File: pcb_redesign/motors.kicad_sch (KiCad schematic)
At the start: 8 parts

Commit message: schematic imported
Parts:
- A3908EEETR-T1, A3908EEETR-T3: footprint (none) -> motor_driver_ic:PSON50P200X300X60-9N
- M1, M3: footprint (none) -> motor:motor
- R4, R8: footprint (none) -> 18k_ohm_0603:RESC1608X55N
- R5, R9: footprint (none) -> 10k_ohm_0603:RESC1508X50N
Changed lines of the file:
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@@
       (effects (font (size 1.27 1.27)))
     )
-    (property "Footprint" "" (at 81.28 123.19 0)
+    (property "Footprint" "motor_driver_ic:PSON50P200X300X60-9N" (at 81.28 123.19 0)
       (effects (font (size 1.27 1.27)) hide)
     )
@@
       (effects (font (size 1.27 1.27)))
     )
-    (property "Footprint" "" (at 82.55 55.88 0)
+    (property "Footprint" "motor_driver_ic:PSON50P200X300X60-9N" (at 82.55 55.88 0)
       (effects (font (size 1.27 1.27)) hide)
     )
@@
       (effects (font (size 1.27 1.27)) (justify left))
     )
-    (property "Footprint" "" (at 54.102 138.43 90)
+    (property "Footprint" "18k_ohm_0603:RESC1608X55N" (at 54.102 138.43 90)
       (effects (font (size 1.27 1.27)) hide)
     )
@@
       (effects (font (size 1.27 1.27)))
     )
-    (property "Footprint" "" (at 114.3 128.27 0)
+    (property "Footprint" "motor:motor" (at 114.3 128.27 0)
       (effects (font (size 1.27 1.27)) hide)
     )
@@
       (effects (font (size 1.27 1.27)))
     )
-    (property "Footprint" "" (at 115.57 60.96 0)
+    (property "Footprint" "motor:motor" (at 115.57 60.96 0)
       (effects (font (size 1.27 1.27)) hide)
     )
@@
       (effects (font (size 1.27 1.27)) (justify left))
     )
-    (property "Footprint" "" (at 54.102 148.59 90)
+    (property "Footprint" "10k_ohm_0603:RESC1508X50N" (at 54.102 148.59 90)
       (effects (font (size 1.27 1.27)) hide)
     )
@@
       (effects (font (size 1.27 1.27)) (justify left))
     )
-    (property "Footprint" "" (at 55.372 81.28 90)
+    (property "Footprint" "10k_ohm_0603:RESC1508X50N" (at 55.372 81.28 90)
       (effects (font (size 1.27 1.27)) hide)
     )
@@
       (effects (font (size 1.27 1.27)) (justify left))
     )
-    (property "Footprint" "" (at 55.372 71.12 90)
-      (effects (font (size 1.27 1.27)) hide)
-    )
+    (property "Footprint" "18k_ohm_0603:RESC1608X55N" (at 55.372 71.12 90)
+      (effects (font (size 1.27 1.27)) hide)
+    )

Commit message: components added to board
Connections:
- net 3.7_UNREG: now reaches A3908EEETR-T3.3 (VDD)
- net 3.7_UNREG: now also A3908EEETR-T1.3 (VDD)
- net ENA Left motor renamed ENA Left Motor
- net ENA Left Motor: no longer A3908EEETR-T3.6 (IN_1)
- net ENA Right motor renamed ENB Right Motor
- net ENB Right motor renamed ENA Right Motor
- new net ENB Left Motor: A3908EEETR-T3.6 (IN_1)
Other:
- moved on the sheet: M3

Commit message: switching to laptop
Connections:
- net 3.7_UNREG: no longer A3908EEETR-T3.3 (VDD)
- new net VCC_3V3: A3908EEETR-T3.3 (VDD)
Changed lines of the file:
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@@
     )
   )
-  (global_label "3.7_UNREG" (shape input) (at 93.98 132.08 0) (fields_autoplaced)
+  (global_label "VCC_3V3" (shape input) (at 93.98 132.08 0) (fields_autoplaced)
     (effects (font (size 1.27 1.27)) (justify left))
-    (property "Intersheetrefs" "${INTERSHEET_REFS}" (at 107.2272 132.08 0)
+    (property "Intersheetrefs" "${INTERSHEET_REFS}" (at 104.9896 132.08 0)
       (effects (font (size 1.27 1.27)) (justify left) hide)
     )

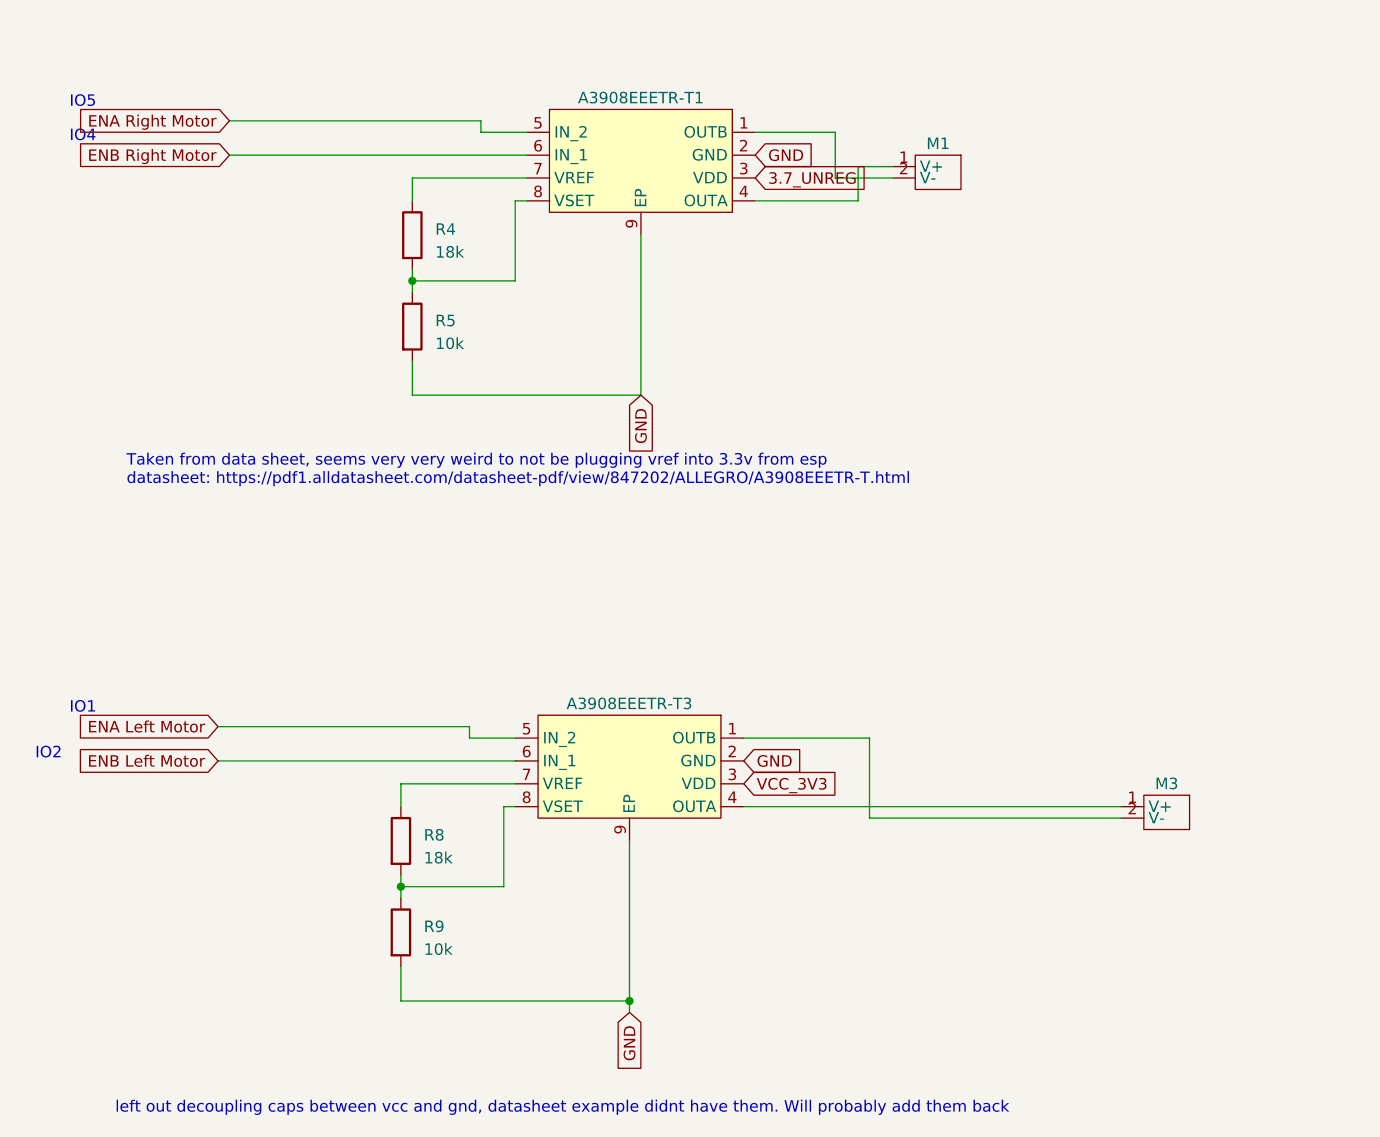
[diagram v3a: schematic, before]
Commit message: wired up 2.13
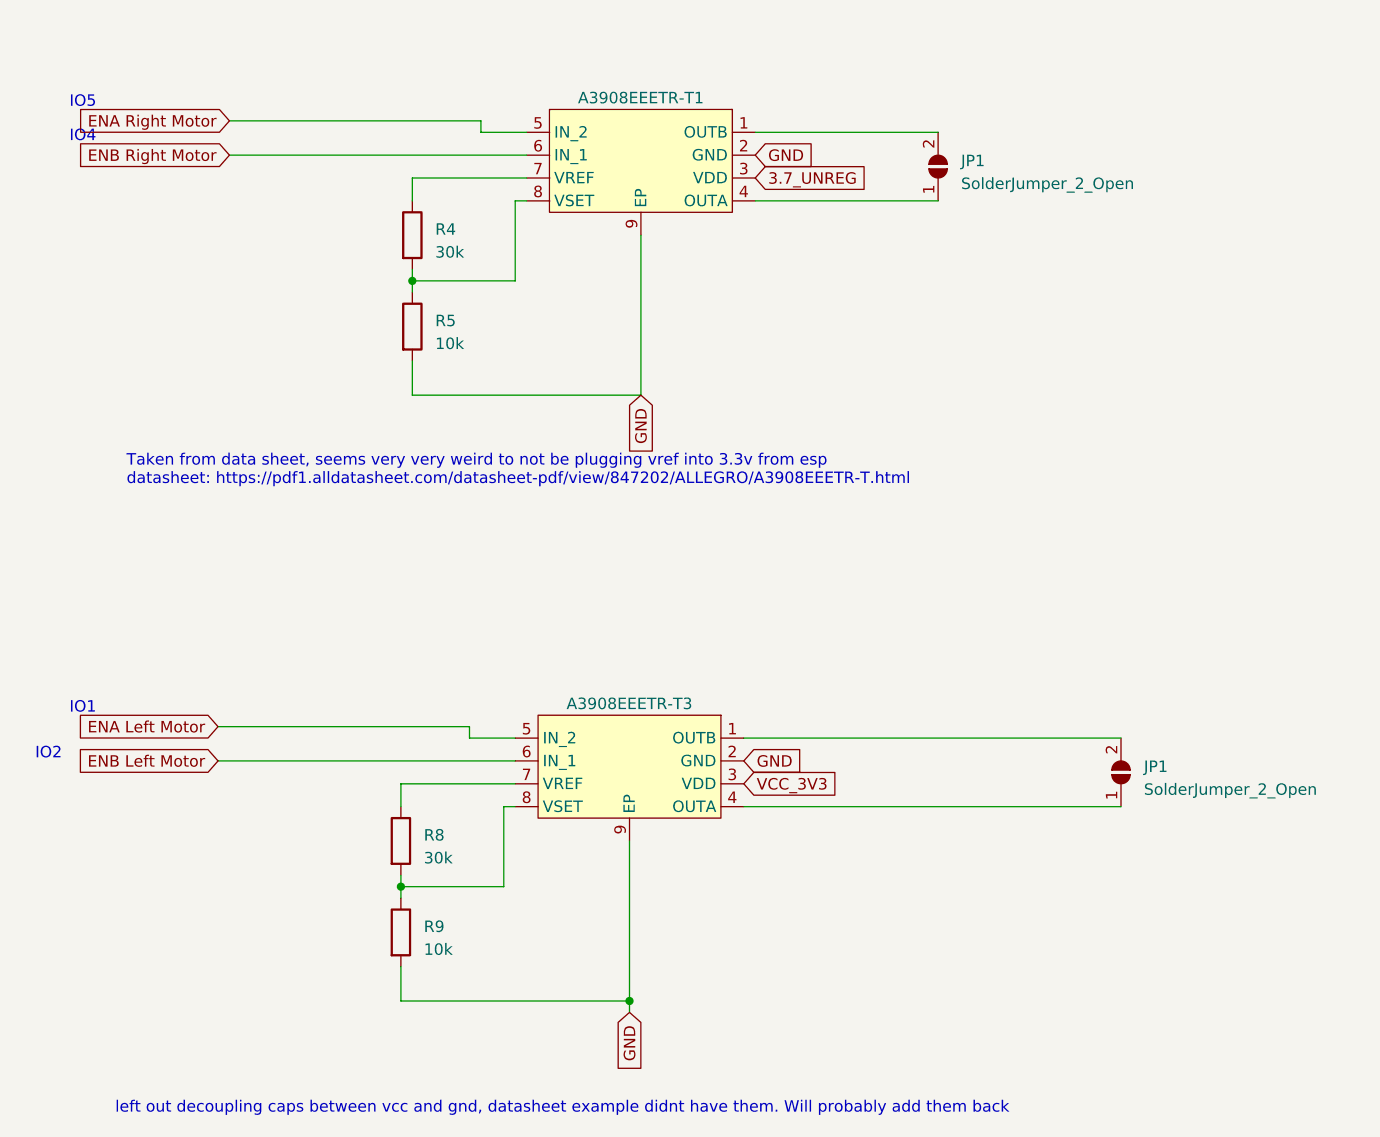
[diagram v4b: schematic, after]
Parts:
- removed M1, M3: ~, motor:motor, symbol lib:motor
- added JP1 (x2): SolderJumper_2_Open, Jumper:SolderJumper-2_P1.3mm_Open_Pad1.0x1.5mm, symbol Jumper:SolderJumper_2_Open
- R4, R8: value 18k -> 30k
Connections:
- net at A3908EEETR-T3.1 (OUTB): now also JP1.2 (B)
- net at A3908EEETR-T3.4 (OUTA): now also JP1.1 (A)
- net at A3908EEETR-T1.1 (OUTB): now also JP1.2 (B)
- net at A3908EEETR-T1.4 (OUTA): now also JP1.1 (A)
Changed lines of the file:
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@@
-    (stroke (width 0) (type default))
-  )
-  (wire (pts (xy 95.25 59.69) (xy 104.14 59.69))
     (stroke (width 0) (type default))
   )
@@
     (stroke (width 0) (type default))
   )
-  (wire (pts (xy 104.14 64.77) (xy 110.49 64.77))
-    (stroke (width 0) (type default))
-  )
   (wire (pts (xy 55.88 142.24) (xy 55.88 143.51))
     (stroke (width 0) (type default))
@@
     (stroke (width 0) (type default))
   )
-  (wire (pts (xy 106.68 67.31) (xy 106.68 63.5))
-    (stroke (width 0) (type default))
-  )
   (wire (pts (xy 64.77 58.42) (xy 64.77 59.69))
     (stroke (width 0) (type default))
   )
-  (wire (pts (xy 95.25 67.31) (xy 106.68 67.31))
+  (wire (pts (xy 95.25 67.31) (xy 115.57 67.31))
     (stroke (width 0) (type default))
   )
@@
     (stroke (width 0) (type default))
   )
-  (wire (pts (xy 106.68 63.5) (xy 110.49 63.5))
-    (stroke (width 0) (type default))
-  )
-  (wire (pts (xy 107.95 127) (xy 107.95 135.89))
-    (stroke (width 0) (type default))
-  )
   (wire (pts (xy 67.31 134.62) (xy 67.31 143.51))
     (stroke (width 0) (type default))
   )
+  (wire (pts (xy 95.25 59.69) (xy 115.57 59.69))
+    (stroke (width 0) (type default))
+  )
   (wire (pts (xy 67.31 143.51) (xy 55.88 143.51))
     (stroke (width 0) (type default))
@@
     (stroke (width 0) (type default))
   )
-  (wire (pts (xy 104.14 59.69) (xy 104.14 64.77))
-    (stroke (width 0) (type default))
-  )
   (wire (pts (xy 57.15 85.09) (xy 57.15 88.9))
     (stroke (width 0) (type default))
   )
-  (wire (pts (xy 93.98 127) (xy 107.95 127))
+  (wire (pts (xy 93.98 127) (xy 135.89 127))
     (stroke (width 0) (type default))
   )
@@
   )
   (wire (pts (xy 55.88 132.08) (xy 55.88 134.62))
-    (stroke (width 0) (type default))
-  )
-  (wire (pts (xy 107.95 135.89) (xy 135.89 135.89))
     (stroke (width 0) (type default))
   )
@@
     )
   )
+  (symbol (lib_id "Jumper:SolderJumper_2_Open") (at 115.57 63.5 90) (unit 1)
+    (in_bom yes) (on_board yes) (dnp no) (fields_autoplaced)
+    (property "Reference" "JP1" (at 118.11 62.865 90)
+      (effects (font (size 1.27 1.27)) (justify right))
+    )
+    (property "Value" "SolderJumper_2_Open" (at 118.11 65.405 90)
+      (effects (font (size 1.27 1.27)) (justify right))
+    )
+    (property "Footprint" "Jumper:SolderJumper-2_P1.3mm_Open_Pad1.0x1.5mm" (at 115.57 63.5 0)
+      (effects (font (size 1.27 1.27)) hide)
+    )
+    (property "Datasheet" "~" (at 115.57 63.5 0)
+      (effects (font (size 1.27 1.27)) hide)
+    )
+    (pin "1")
+    (pin "2")
+    (instances
+      (project "pcb_redesign"
+        (path "/fb030e39-7dd3-46a0-8379-c26b3ef1b0a0"
+          (reference "JP1") (unit 1)
+        )
+        (path "/fb030e39-7dd3-46a0-8379-c26b3ef1b0a0/6a7629e6-5379-48e0-a979-c6c26844d2b7"
+          (reference "JP2") (unit 1)
+        )
+      )
+    )
+  )
   (symbol (lib_id "lib:Motor_IC") (at 82.55 55.88 0) (mirror y) (unit 1)
     (in_bom yes) (on_board yes) (dnp no)
@@
       (effects (font (size 1.27 1.27)) (justify left))
     )
-    (property "Value" "18k" (at 58.42 140.335 0)
+    (property "Value" "30k" (at 58.42 140.335 0)
       (effects (font (size 1.27 1.27)) (justify left))
     )
@@
     )
   )
-  (symbol (lib_id "lib:motor") (at 140.97 132.08 0) (mirror y) (unit 1)
-    (in_bom yes) (on_board yes) (dnp no)
-    (property "Reference" "M3" (at 140.97 132.08 0)
-      (effects (font (size 1.27 1.27)))
-    )
-    (property "Value" "~" (at 140.97 132.08 0)
-      (effects (font (size 1.27 1.27)))
-    )
-    (property "Footprint" "motor:motor" (at 140.97 132.08 0)
-      (effects (font (size 1.27 1.27)) hide)
-    )
-    (property "Datasheet" "" (at 140.97 132.08 0)
-      (effects (font (size 1.27 1.27)) hide)
-    )
-    (pin "1")
-    (pin "2")
-    (instances
-      (project "pcb_redesign"
-        (path "/fb030e39-7dd3-46a0-8379-c26b3ef1b0a0/6a7629e6-5379-48e0-a979-c6c26844d2b7"
-          (reference "M3") (unit 1)
-        )
-      )
-    )
-  )
-  (symbol (lib_id "lib:motor") (at 115.57 60.96 0) (mirror y) (unit 1)
-    (in_bom yes) (on_board yes) (dnp no)
-    (property "Reference" "M1" (at 115.57 60.96 0)
-      (effects (font (size 1.27 1.27)))
-    )
-    (property "Value" "~" (at 115.57 60.96 0)
-      (effects (font (size 1.27 1.27)))
-    )
-    (property "Footprint" "motor:motor" (at 115.57 60.96 0)
-      (effects (font (size 1.27 1.27)) hide)
-    )
-    (property "Datasheet" "" (at 115.57 60.96 0)
-      (effects (font (size 1.27 1.27)) hide)
-    )
-    (pin "1")
-    (pin "2")
-    (instances
-      (project "pcb_redesign"
-        (path "/fb030e39-7dd3-46a0-8379-c26b3ef1b0a0/6a7629e6-5379-48e0-a979-c6c26844d2b7"
-          (reference "M1") (unit 1)
-        )
-      )
-    )
-  )
   (symbol (lib_id "Device:R") (at 55.88 148.59 0) (unit 1)
     (in_bom yes) (on_board yes) (dnp no) (fields_autoplaced)
@@
       (effects (font (size 1.27 1.27)) (justify left))
     )
-    (property "Value" "18k" (at 59.69 73.025 0)
+    (property "Value" "30k" (at 59.69 73.025 0)
       (effects (font (size 1.27 1.27)) (justify left))
     )
@@
         )
       )
+    )
+  )
+  (symbol (lib_id "Jumper:SolderJumper_2_Open") (at 135.89 130.81 90) (unit 1)
+    (in_bom yes) (on_board yes) (dnp no) (fields_autoplaced)
+    (property "Reference" "JP1" (at 138.43 130.175 90)
+      (effects (font (size 1.27 1.27)) (justify right))
+    )
+    (property "Value" "SolderJumper_2_Open" (at 138.43 132.715 90)
+      (effects (font (size 1.27 1.27)) (justify right))
+    )
+    (property "Footprint" "Jumper:SolderJumper-2_P1.3mm_Open_Pad1.0x1.5mm" (at 135.89 130.81 0)
+      (effects (font (size 1.27 1.27)) hide)
+    )
+    (property "Datasheet" "~" (at 135.89 130.81 0)
+      (effects (font (size 1.27 1.27)) hide)
+    )
+    (pin "1")
+    (pin "2")
+    (instances
+      (project "pcb_redesign"
+        (path "/fb030e39-7dd3-46a0-8379-c26b3ef1b0a0"
+          (reference "JP1") (unit 1)
+        )
+        (path "/fb030e39-7dd3-46a0-8379-c26b3ef1b0a0/6a7629e6-5379-48e0-a979-c6c26844d2b7"
+          (reference "JP3") (unit 1)
+        )
+      )

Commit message: finished design
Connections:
- net 3.7_UNREG is gone; now on net VCC_3V3: A3908EEETR-T1.3 (VDD)
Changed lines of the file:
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@@
+    )
+  )
+  (global_label "VCC_3V3" (shape input) (at 95.25 64.77 0) (fields_autoplaced)
+    (effects (font (size 1.27 1.27)) (justify left))
+    (property "Intersheetrefs" "${INTERSHEET_REFS}" (at 106.2596 64.77 0)
+      (effects (font (size 1.27 1.27)) (justify left) hide)
     )
   )
@@
     )
   )
-  (global_label "3.7_UNREG" (shape input) (at 95.25 64.77 0) (fields_autoplaced)
-    (effects (font (size 1.27 1.27)) (justify left))
-    (property "Intersheetrefs" "${INTERSHEET_REFS}" (at 108.4972 64.77 0)
-      (effects (font (size 1.27 1.27)) (justify left) hide)
-    )
-  )
